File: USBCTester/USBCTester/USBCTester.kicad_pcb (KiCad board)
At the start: 4 copper layers, 108.6 x 85.1 mm, 77 parts, among them J2 2388749-1, J3 Conn_01x12, J4 Conn_01x03, J5 2388749-1, J6 Conn_01x03, SW1 SW_Push, U1 74HC595, U2 74HC595, U3 74HC595, U4 74HC595, U5 74HC595, U6 74HC595, U7 RaspberryPi_Pico

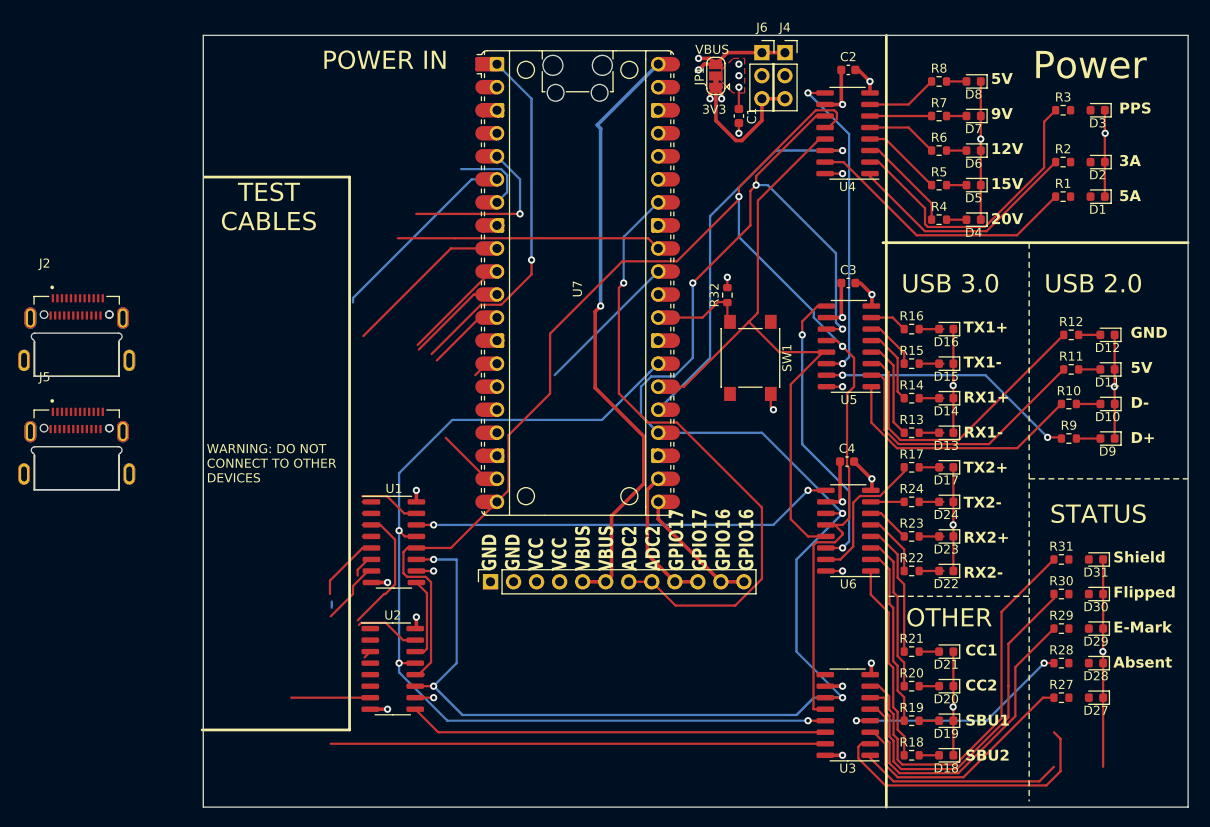
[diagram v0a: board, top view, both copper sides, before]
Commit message: switch to USB4080 footprint
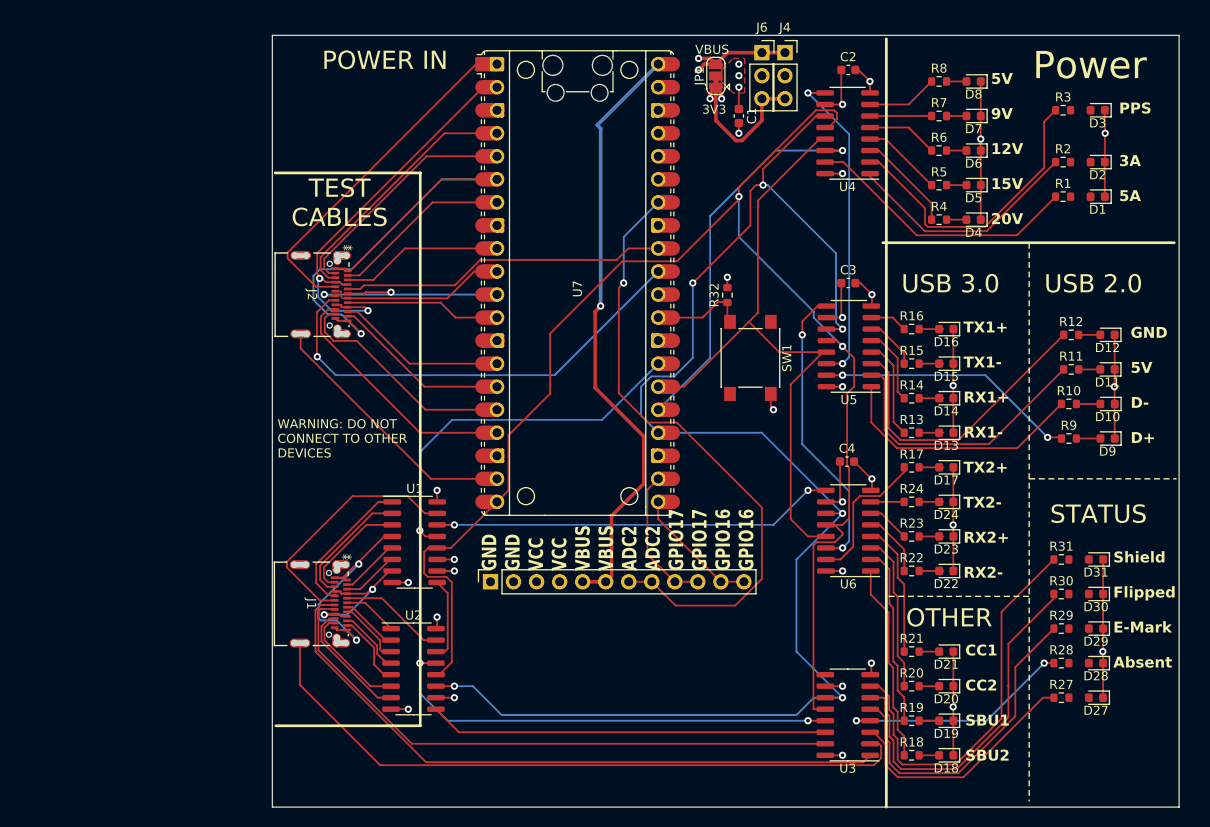
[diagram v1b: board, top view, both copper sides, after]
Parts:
- removed J5: 2388749-1, USBCFootprint:USBC2
- added J1: USB4080-03-A, USBCFootprint:USB4080-03-A_GCT, F.Cu at (123.0, 124.3)
- J2: value 2388749-1 -> USB4080-03-A; footprint USBCFootprint:USBC2 -> USBCFootprint:USB4080-03-A_GCT
- moved J2 26.0 mm to (123.1, 90.2), turned to -90 degrees
- moved U1 2.29 mm to (134.4, 117.5)
- moved U2 2.29 mm to (134.3, 131.4)
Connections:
- J2 pad A1: Net-(U7-GPIO11) -> Net-(U7-GPIO4)
- J2 pad A12: Net-(U7-GPIO11) -> Net-(U7-GPIO4)
- J2 pad A4: Net-(U7-GPIO3) -> Net-(U7-GPIO1)
- J2 pad A9: Net-(U7-GPIO3) -> Net-(U7-GPIO1)
- J2 pad B1: Net-(U7-GPIO11) -> Net-(U7-GPIO4)
- J2 pad B12: Net-(U7-GPIO11) -> Net-(U7-GPIO4)
- J2 pad B4: Net-(U7-GPIO3) -> Net-(U7-GPIO1)
- J2 pad B9: Net-(U7-GPIO3) -> Net-(U7-GPIO1)
- U1 pad 14: unconnected-(U1-SER-Pad14) -> Net-(U1-SER)
- U6 pad 9: unconnected-(U6-QH'-Pad9) -> Net-(U1-SER)
- U7 pad 11: Net-(J2-SBU1) -> Net-(J2-DP1)
- U7 pad 12: Net-(J2-SSRXN2) -> Net-(J2-SBU1)
- U7 pad 14: Net-(J2-SSRXP2) -> Net-(J2-SSRXN2)
- U7 pad 15: Net-(U7-GPIO11) -> Net-(J2-SSRXP2)
- U7 pad 2: Net-(J2-SSRXN1) -> Net-(U7-GPIO1)
- U7 pad 31: Net-(J2-CC1) -> Net-(J2-CC2)
- U7 pad 32: Net-(J2-CC2) -> Net-(J2-CC1)
- U7 pad 4: Net-(J2-SSRXP1) -> Net-(J2-SSRXN1)
- U7 pad 5: Net-(U7-GPIO3) -> Net-(J2-SSRXP1)
- U7 pad 6: Net-(J2-SSTXP1) -> Net-(U7-GPIO4)
- U7 pad 7: Net-(J2-SSTXN1) -> Net-(J2-SSTXP1)
- U7 pad 9: Net-(J2-DP1) -> Net-(J2-SSTXN1)
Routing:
- net Net-(U7-GPIO4): track 0.00 -> 59.7 mm, vias 0 -> 1
- net Net-(J1-DP2): track 22.3 -> 73.8 mm
- net Net-(U7-GPIO1): track 0.00 -> 47.4 mm, vias 0 -> 2
- net (no net): track 47.4 -> 0.00 mm, vias 2 -> 0
- net Net-(U1-SER): track 0.00 -> 44.4 mm, vias 0 -> 2
- net Net-(U3-QC): track 31.5 -> 75.9 mm
- net Net-(J2-SSTXN2): track 0.00 -> 27.8 mm
- net Net-(J2-SSRXN1): track 1.13 -> 28.5 mm
- net Net-(J2-SSRXP1): track 0.65 -> 26.9 mm
- net Net-(J2-SSTXP2): track 0.00 -> 25.4 mm
- net Net-(U1-QE): track 0.97 -> 26.2 mm, vias 0 -> 2
- net Net-(J2-CC2): track 29.2 -> 50.7 mm, vias 0 -> 1
- net Net-(U7-GPIO14): track 7.53 -> 28.8 mm
- net Net-(J1-DN2): track 6.76 -> 27.7 mm
- net SRCLK: track 189.7 -> 169.5 mm
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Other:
- board size 108.6 x 85.1 mm -> 100 x 85.1 mm

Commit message: add protoboard, lots of tweaks and silkscreen improvements
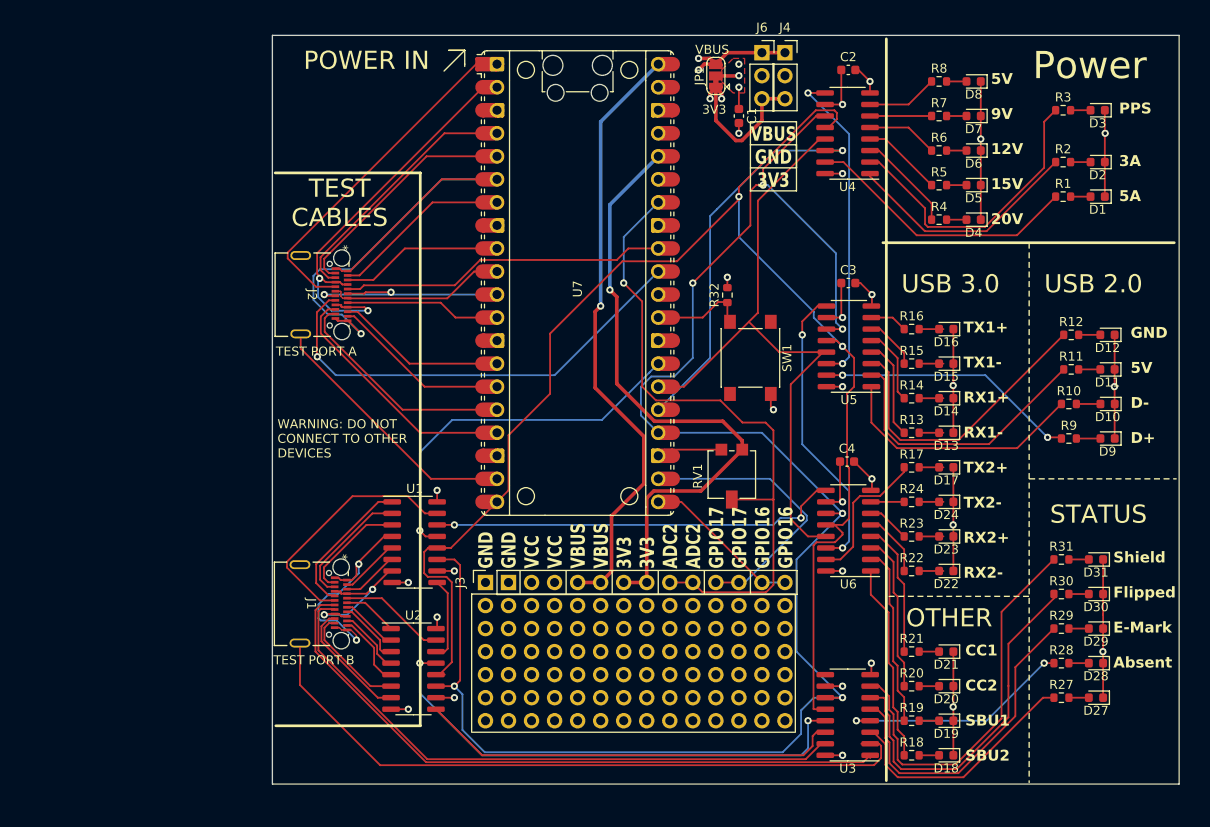
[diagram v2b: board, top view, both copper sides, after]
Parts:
- added PB1: ~, ProtoBoard:ProtoBoard 14x6, F.Cu at (154.9, 119.4)
- added RV1: R_Potentiometer, Potentiometer_SMD:Potentiometer_Vishay_TS53YL_Vertical, F.Cu at (169.4, 110.0)
- J1, J2: footprint USBCFootprint:USB4080-03-A_GCT -> USBCFootprint:USB4080-03-A_GCT_RoundHoles
- J3: value Conn_01x12 -> Conn_01x14; footprint Connector_PinSocket_2.54mm:PinSocket_1x12_P2.54mm_Vertical -> Connector_PinSocket_2.54mm:PinSocket_1x14_P2.54mm_Vertical
- moved J3 0.56 mm to (142.2, 121.9)
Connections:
- J3 pad 10: GPIO17 -> GPIO28
- J3 pad 11: GPIO16 -> GPIO17
- J3 pad 12: GPIO16 -> GPIO17
- J3 pad 7: GPIO28 -> +3V3
- J3 pad 8: GPIO28 -> +3V3
- J3 pad 9: GPIO17 -> GPIO28
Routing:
- net +3V3: track 18.4 -> 88.0 mm, vias 2 -> 3
- net SRCLK: track 169.5 -> 191.3 mm, vias 7 -> 6
- net GPIO17: track 15.6 -> 31.4 mm
- net GND: track 104.2 -> 111.5 mm
- net Net-(U1-~{OE}): track 106.8 -> 111.7 mm
- net GPIO28: track 68.7 -> 73.0 mm
- net GPIO16: track 14.2 -> 17.7 mm
- net Net-(U2-QH'): track 44.0 -> 46.7 mm
- net VCC: track 38.5 -> 41.0 mm
- net Net-(D31-A): track 0.00 -> 2.20 mm
- net Net-(D30-A): track 0.00 -> 2.20 mm
- net Net-(D3-A): track 0.00 -> 2.20 mm
- net Net-(D29-A): track 0.00 -> 2.20 mm
- net Net-(D28-A): track 0.00 -> 2.20 mm
- net Net-(D27-A): track 0.00 -> 2.20 mm
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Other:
- board size 100 x 85.1 mm -> 100 x 82.6 mm
- board text added: "GND GND VCC VCC VBUS VBUS 3V3 3V3 ADC2 ADC2 GPIO17 GPIO17 GPIO16 GPIO16"
- board text added: "TEST PORT A"
- board text added: "TEST PORT B"
- board text added: "TODO RESOLVE DRC ERRORS ADD MOUNTING HOLES ADD NAME, REV, ETC"
- board text added: "VBUS GND 3V3"
- board text removed: "GND GND VCC VCC VBUS VBUS ADC2 ADC2 GPIO17 GPIO17 GPIO16 GPIO16"
- board text removed: "TODO ADD PROTOBOARD SPACE HERE. MAYBE ALSO POT FOOTPRINT FOR VOLTAGE SELECTION RESOLVE DRC ERRORS ADD NAME, REV, ETC"

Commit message: many tweaks to finalize design, then Schematic update for safety with external devices
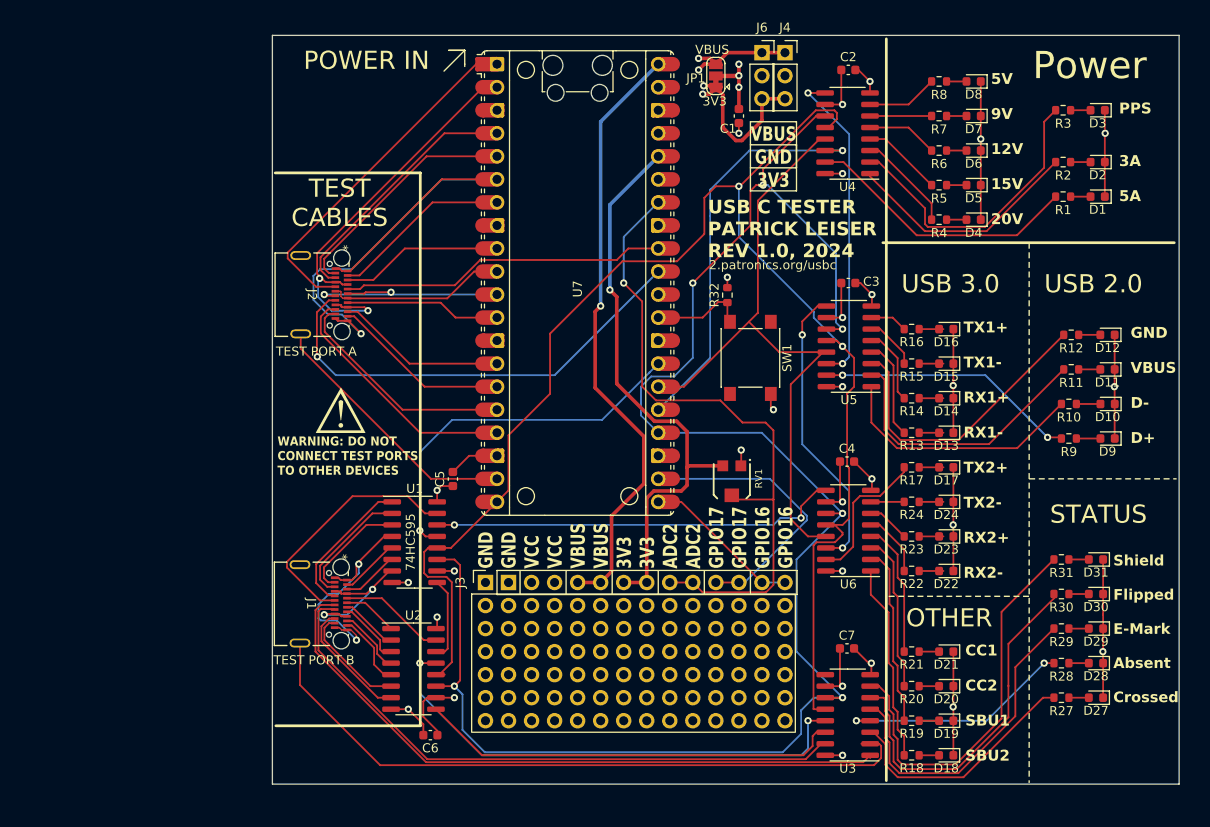
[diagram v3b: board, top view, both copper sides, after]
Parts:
- added C5: C, Capacitor_SMD:C_0603_1608Metric, F.Cu at (138.6, 110.5)
- added C6: C, Capacitor_SMD:C_0603_1608Metric, F.Cu at (136.2, 138.8)
- added C7: C, Capacitor_SMD:C_0603_1608Metric, F.Cu at (182.1, 129.2)
- added G***: LOGO, USBCFootprint:SilkScreenReference, B.Cu at (202.6, 102.2)
- R32: value R -> 10k
- RV1: footprint Potentiometer_SMD:Potentiometer_Vishay_TS53YL_Vertical -> Potentiometer_SMD:TRIM_35WR10KLFTR
- moved RV1 0.64 mm to (169.4, 110.7), turned to -90 degrees
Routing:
- net VCC: track 41.0 -> 55.6 mm
- net GND: track 111.5 -> 118.7 mm, vias 15 -> 16
- net +3V3: track 88.0 -> 83.0 mm
- net RCLK: track 166.1 -> 168.5 mm
- net Net-(U4-SER): track 45.0 -> 46.7 mm
- removed copper zone on F.Cu, net VCC
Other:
- board text added: "2.patronics.org/usbc"
- board text added: "74HC595"
- board text added: "GND VBUS D- D+"
- board text added: "Shield Flipped E-Mark Absent Crossed"
- board text added: "USB C TESTER PATRICK LEISER REV 1.0, 2024"
- board text added: "WARNING: DO NOT CONNECT TEST PORTS TO OTHER DEVICES"
- board text added: "⚠"
- board text removed: "GND 5V D- D+"
- board text removed: "Shield Flipped E-Mark Absent"
- board text removed: "WARNING: DO NOT CONNECT TO OTHER DEVICES"

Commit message: update layout with improved external device safety and testing for active cables
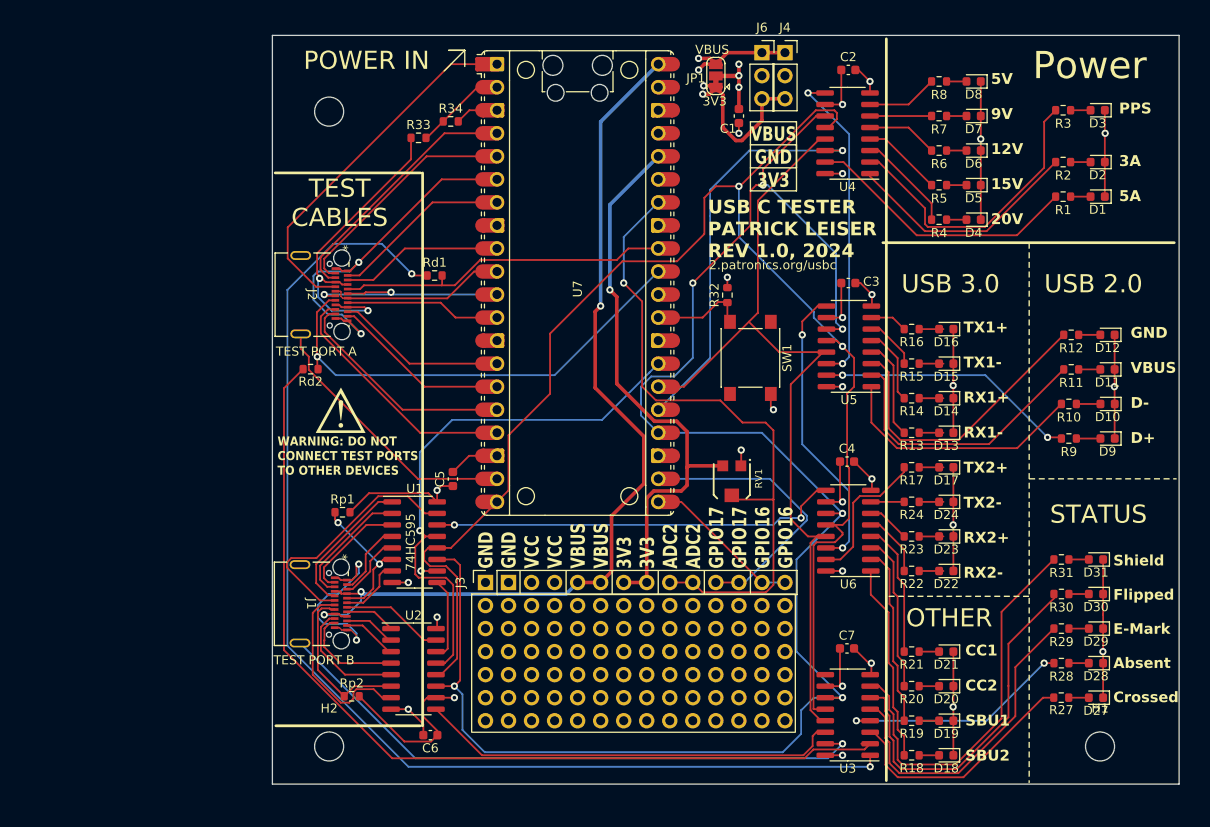
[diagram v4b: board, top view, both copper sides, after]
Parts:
- added H1: MountingHole, MountingHole:MountingHole_3.2mm_M3, F.Cu at (210.0, 140.0)
- added H2: MountingHole, MountingHole:MountingHole_3.2mm_M3, F.Cu at (125.0, 140.0)
- added H3: MountingHole, MountingHole:MountingHole_3.2mm_M3, F.Cu at (125.0, 70.0)
- added R33: 6.8k, Resistor_SMD:R_0603_1608Metric, F.Cu at (134.9, 72.9)
- added R34: 12k, Resistor_SMD:R_0603_1608Metric, F.Cu at (138.4, 71.1)
- added Rd1: 5k1, Resistor_SMD:R_0603_1608Metric, F.Cu at (136.6, 88.1)
- added Rd2: 5k1, Resistor_SMD:R_0603_1608Metric, F.Cu at (123.0, 98.4)
- added Rp1: 36k, Resistor_SMD:R_0603_1608Metric, F.Cu at (126.5, 114.2)
- added Rp2: 36k, Resistor_SMD:R_0603_1608Metric, F.Cu at (127.5, 134.5)
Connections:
- J1 pad 27: Net-(U3-QC) -> Net-(U3-QA)
- J1 pad 28: Net-(U3-QC) -> Net-(U3-QA)
- J1 pad A1: Net-(U1-QE) -> GND
- J1 pad A12: Net-(U1-QE) -> GND
- J1 pad A4: Net-(U1-QH) -> VBUS
- J1 pad A9: Net-(U1-QH) -> VBUS
- J1 pad B1: Net-(U1-QE) -> GND
- J1 pad B12: Net-(U1-QE) -> GND
- J1 pad B4: Net-(U1-QH) -> VBUS
- J1 pad B9: Net-(U1-QH) -> VBUS
- J2 pad A4: Net-(U7-GPIO1) -> Net-(J2-VBUS-PadA4)
- J2 pad A9: Net-(U7-GPIO1) -> Net-(J2-VBUS-PadA4)
- J2 pad B4: Net-(U7-GPIO1) -> Net-(J2-VBUS-PadA4)
- J2 pad B9: Net-(U7-GPIO1) -> Net-(J2-VBUS-PadA4)
- U1 pad 4: Net-(U1-QE) -> Net-(J1-SSTXP1)
- U1 pad 5: Net-(J1-SSTXP1) -> Net-(J1-SSTXN1)
- U1 pad 6: Net-(J1-SSTXN1) -> Net-(J1-CC1)
- U1 pad 7: Net-(U1-QH) -> Net-(J1-DP1)
- U2 pad 1: Net-(J1-DP1) -> Net-(J1-SBU1)
- U2 pad 15: Net-(J1-CC1) -> Net-(J1-DN1)
- U2 pad 2: Net-(J1-DN1) -> Net-(J1-SSRXN2)
- U2 pad 3: Net-(J1-SBU1) -> Net-(J1-SSRXP2)
- U2 pad 4: Net-(J1-SSRXN2) -> Net-(J1-SSTXP2)
- U2 pad 5: Net-(J1-SSRXP2) -> Net-(J1-SSTXN2)
- U2 pad 6: Net-(J1-SSTXP2) -> Net-(J1-CC2)
- U2 pad 7: Net-(J1-SSTXN2) -> Net-(J1-DP2)
- U3 pad 1: Net-(J1-DP2) -> Net-(U3-QB)
- U3 pad 13: Net-(U1-~{OE}) -> Net-(U3-~{OE})
- U3 pad 15: Net-(J1-CC2) -> Net-(U3-QA)
- U4 pad 13: Net-(U4-~{OE}) -> Net-(U3-~{OE})
- U5 pad 13: Net-(U4-~{OE}) -> Net-(U3-~{OE})
- U6 pad 13: Net-(U4-~{OE}) -> Net-(U3-~{OE})
- U7 pad 26: Net-(U4-~{OE}) -> Net-(U3-~{OE})
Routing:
- net Net-(U3-QB): track 0.00 -> 129.2 mm, vias 0 -> 2
- net Net-(U3-~{OE}): track 0.00 -> 94.4 mm
- net Net-(U4-~{OE}): track 71.8 -> 0.00 mm
- net Net-(U3-QA): track 0.00 -> 67.2 mm, vias 0 -> 1
- net Net-(J1-DP2): track 73.8 -> 20.9 mm
- net Net-(U1-~{OE}): track 111.7 -> 61.4 mm, vias 3 -> 1
- net Net-(J1-CC2): track 67.8 -> 18.2 mm
- net Net-(U7-GPIO1): track 45.9 -> 10.1 mm, vias 2 -> 0
- net VBUS: track 79.2 -> 115.0 mm, vias 3 -> 5
- net Net-(J2-VBUS-PadA4): track 0.00 -> 34.7 mm, vias 0 -> 2
- net Net-(U3-QC): track 75.9 -> 103.1 mm
- net GND: track 118.7 -> 145.5 mm, vias 16 -> 18
- net Net-(U1-QE): track 26.4 -> 0.00 mm, vias 2 -> 0
- net VCC: track 55.6 -> 77.4 mm
- net Net-(U7-GPIO4): track 59.7 -> 40.7 mm, vias 1 -> 2
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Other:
- board text removed: "TODO RESOLVE DRC ERRORS ADD MOUNTING HOLES ADD NAME, REV, ETC"

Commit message: pretty and useful back silkscreen
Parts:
- added G***: LOGO, LOGO, B.Cu at (158.8, 93.9)
